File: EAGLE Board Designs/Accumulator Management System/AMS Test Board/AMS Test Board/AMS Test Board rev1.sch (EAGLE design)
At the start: 43 parts, among them J1 CONNECTOR-2__B2B-PH-K, J10 CONNECTOR-2__B2B-PH-K, J11 CONNECTOR-2__B2B-PH-K, J12 CONNECTOR-2__B2B-PH-K, J13 CONNECTOR-2__B2B-PH-K, J14 CONNECTOR-2__B2B-PH-K, J15 CONNECTOR-2__B2B-PH-K, J16 CONNECTOR-2__B2B-PH-K, J17 CONNECTOR-2__B2B-PH-K, J18 CONNECTOR-2__B2B-PH-K, J19 CONNECTOR-2__B2B-PH-K, J2 CONNECTOR-2__B2B-PH-K, J20 CONNECTOR-2__B2B-PH-K, J21 CONNECTOR-2__B2B-PH-K, J22 CONNECTOR-1_5222, J23 CONNECTOR-1_5222, J24 CONNECTOR-1_5222, J25 CONNECTOR-1_5222, J26 CONNECTOR-1_5222, J27 CONNECTOR-1_5222, J28 CONNECTOR-1_5222, J29 CONNECTOR-1_5222, J3 CONNECTOR-2__B2B-PH-K, J30 CONNECTOR-1_5222, J31 CONNECTOR-1_5222, J32 CONNECTOR-1_5222, J33 CONNECTOR-1_5222, J34 CONNECTOR-1_5222, J35 CONNECTOR-1_5222, J36 CONNECTOR-1_5222, J37 CONNECTOR-1_5222, J38 CONNECTOR-1_5222, J39 CONNECTOR-1_5222, J4 CONNECTOR-2__B2B-PH-K, J40 CONNECTOR-1_5222, J41 CONNECTOR-1_5222, J42 CONNECTOR-1_5222, J43 CONNECTOR-1_5222, J5 CONNECTOR-2__B2B-PH-K, J6 CONNECTOR-2__B2B-PH-K, J7 CONNECTOR-2__B2B-PH-K, J8 CONNECTOR-2__B2B-PH-K, J9 CONNECTOR-2__B2B-PH-K

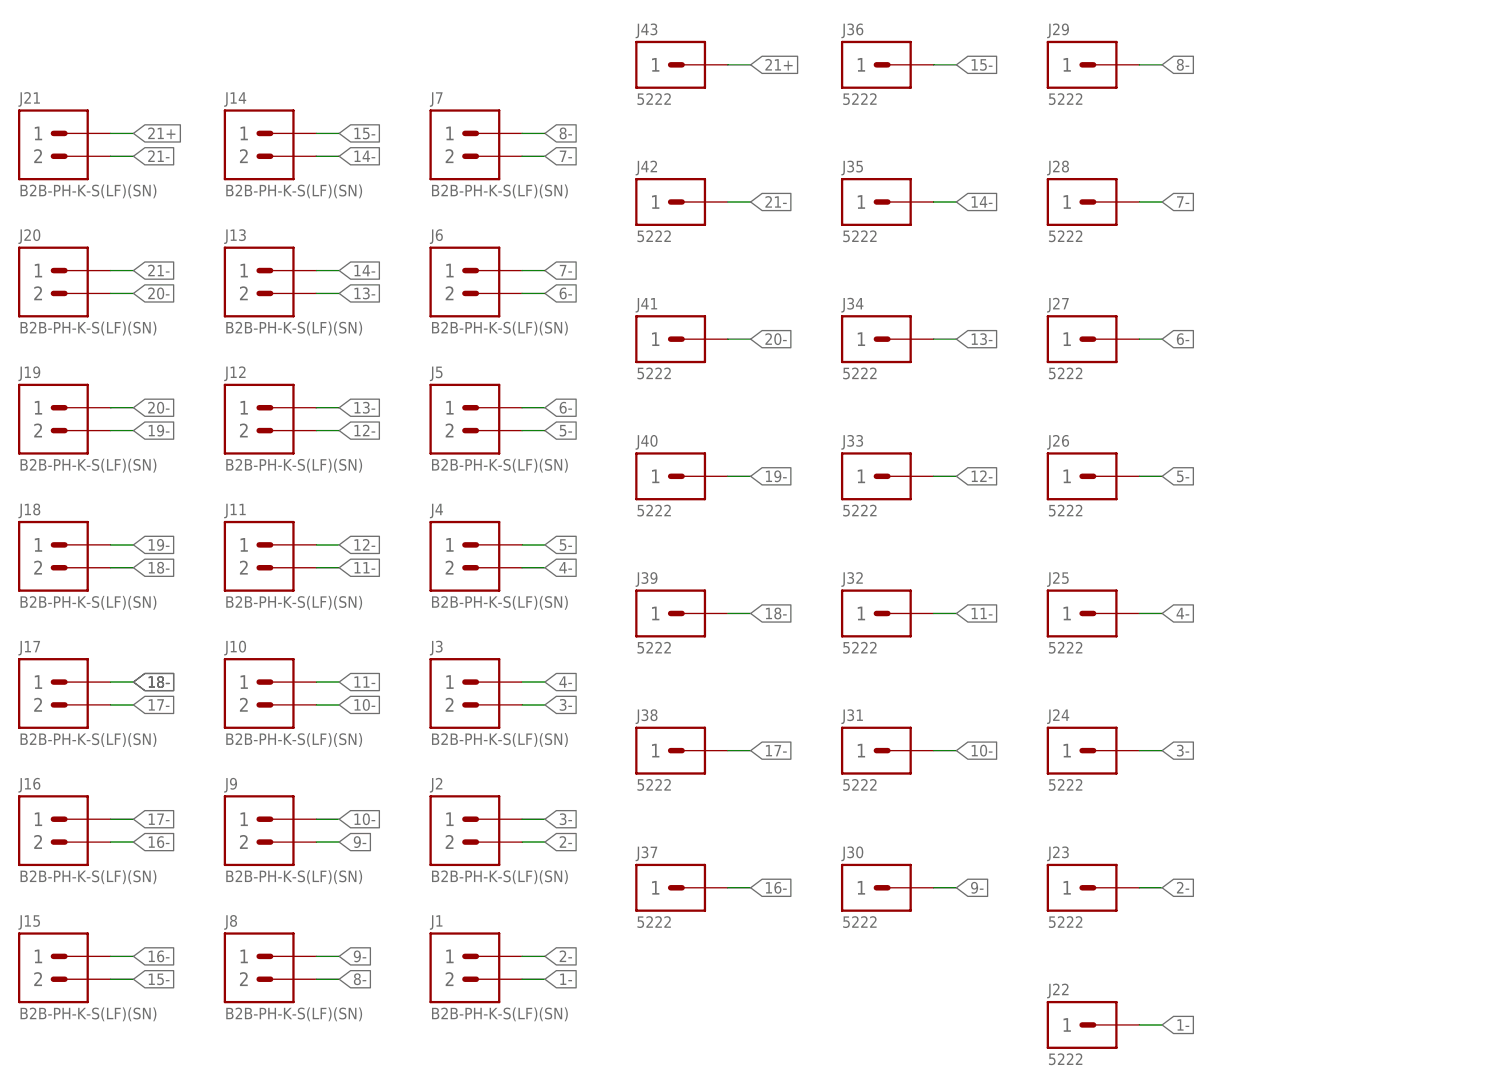
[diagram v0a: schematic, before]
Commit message: AMS Test Board Update
Created additional space between battery connectors and added fuses.
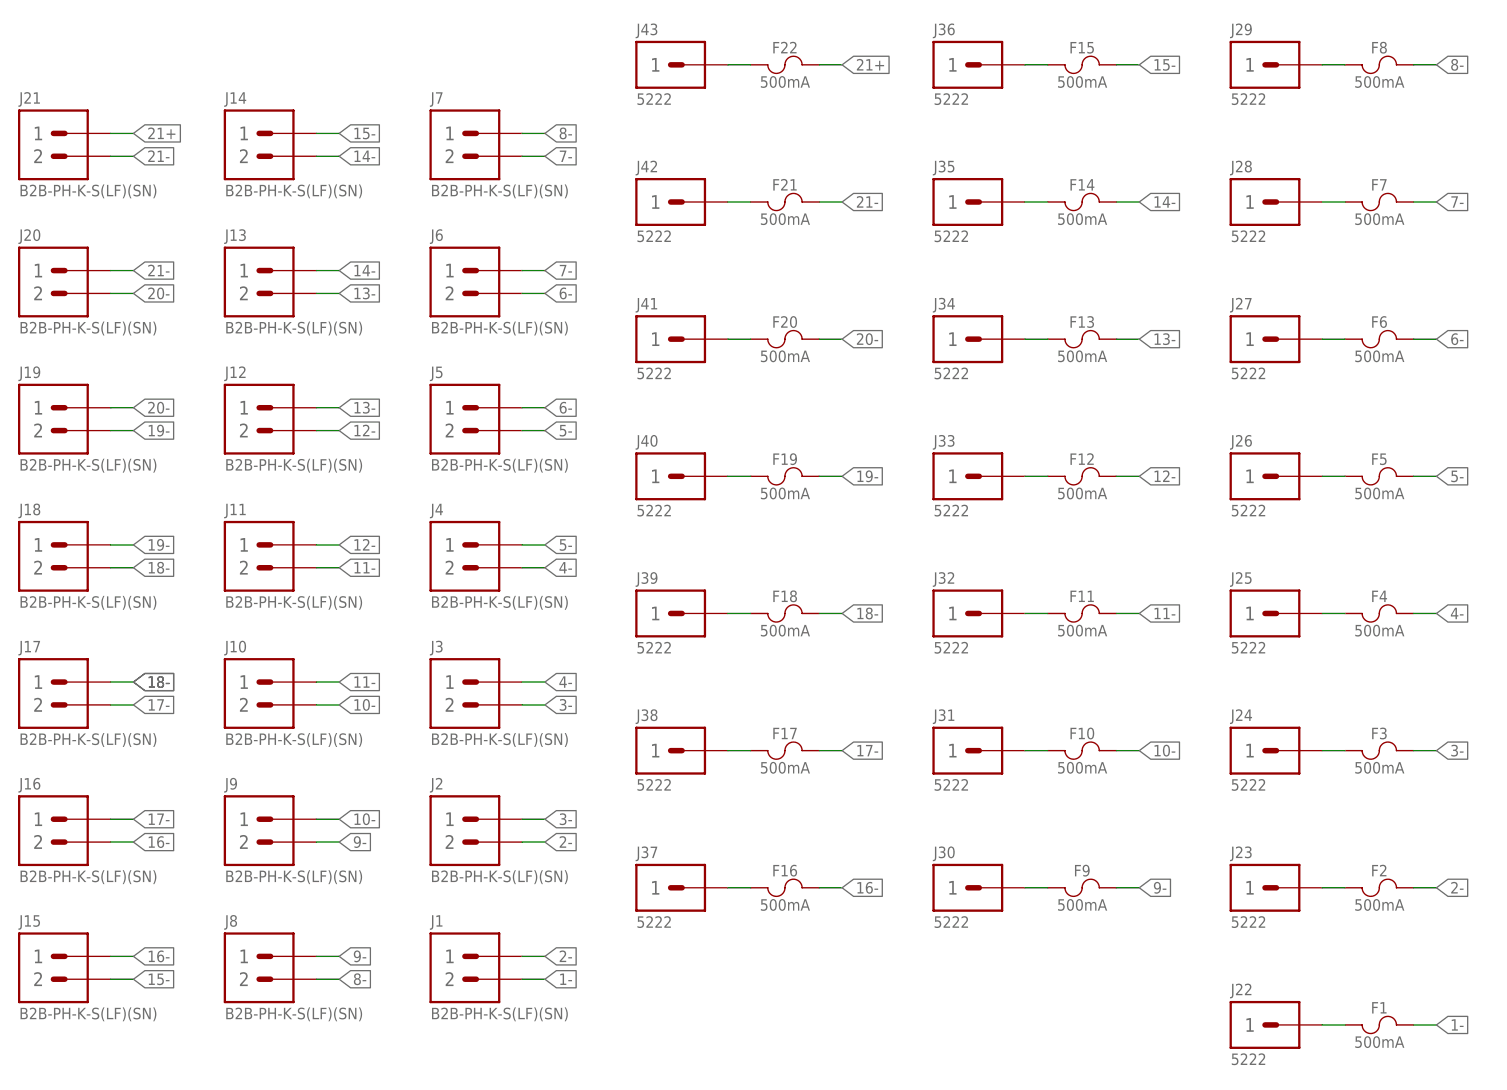
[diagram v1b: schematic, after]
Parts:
- added F1, F10, F11, F12, F13, F14, F15, F16, F17, F18, F19, F2, F20, F21, F22, F3, F4, F5, F6, F7, F8, F9: FUSE_OMF_125_.5A, HyTechDevices:FUSE_OMF_125_.5A
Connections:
- new net N$1: F1.1, J22.1
- new net N$10: F10.1, J31.1
- new net N$11: F11.1, J32.1
- new net N$12: F12.1, J33.1
- new net N$13: F13.1, J34.1
- new net N$14: F14.1, J35.1
- new net N$15: F15.1, J36.1
- new net N$16: F16.1, J37.1
- new net N$17: F17.1, J38.1
- new net N$18: F18.1, J39.1
- new net N$19: F19.1, J40.1
- new net N$2: F2.1, J23.1
- new net N$20: F20.1, J41.1
- new net N$21: F21.1, J42.1
- new net N$22: F22.1, J43.1
- new net N$3: F3.1, J24.1
- new net N$4: F4.1, J25.1
- new net N$5: F5.1, J26.1
- new net N$6: F6.1, J27.1
- new net N$7: F7.1, J28.1
- new net N$8: F8.1, J29.1
- new net N$9: F9.1, J30.1
- net 1-: now also F1.2; no longer J22.1
- net 10-: now also F10.2; no longer J31.1
- net 11-: now also F11.2; no longer J32.1
- net 12-: now also F12.2; no longer J33.1
- net 13-: now also F13.2; no longer J34.1
- net 14-: now also F14.2; no longer J35.1
- net 15-: now also F15.2; no longer J36.1
- net 16-: now also F16.2; no longer J37.1
- net 17-: now also F17.2; no longer J38.1
- net 18-: now also F18.2; no longer J39.1
- net 19-: now also F19.2; no longer J40.1
- net 2-: now also F2.2; no longer J23.1
- net 20-: now also F20.2; no longer J41.1
- net 21+: now also F22.2; no longer J43.1
- net 21-: now also F21.2; no longer J42.1
- net 3-: now also F3.2; no longer J24.1
- net 4-: now also F4.2; no longer J25.1
- net 5-: now also F5.2; no longer J26.1
- net 6-: now also F6.2; no longer J27.1
- net 7-: now also F7.2; no longer J28.1
- net 8-: now also F8.2; no longer J29.1
- net 9-: now also F9.2; no longer J30.1
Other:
- moved on the sheet: J22, J23, J24, J25, J26, J27, J28, J29, J30, J31, J32, J33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
